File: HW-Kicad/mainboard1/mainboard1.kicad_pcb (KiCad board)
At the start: 2 copper layers, 101 x 101 mm, 17 parts, among them J1 Conn_01x03_Male, J2 Conn_01x02_Male, J3 Conn_01x07_Male, J4 Conn_01x04_Male, J5 Conn_01x04_Male, J8 Conn_02x10_Odd_Even, U1 MCP1700-2802E_TO92, U2 ESP32-WROOM-E, U3 Mini360, U4 YAAJ_DCDC_StepDown_LM2596

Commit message: agregue texto para foto
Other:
- board text added: "10v Rx Tx GND"
- board text added: "GND TX RX 10V"
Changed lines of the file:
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@@
   (gr_line (start 214.24 140.7) (end 119.24 140.7) (layer "Edge.Cuts") (width 0.2))
   (gr_circle (center 207.365 43.825) (end 208.865 43.825) (layer "Edge.Cuts") (width 0.2) (fill none))
+  (gr_text "10v\nRx\nTx\nGND" (at 192.7 47.2) (layer "B.SilkS")
+    (effects (font (size 2 2) (thickness 0.15)) (justify mirror))
+  )
+  (gr_text "GND\nTX\nRX\n10V" (at 142.4 47.6) (layer "B.SilkS")
+    (effects (font (size 2 2) (thickness 0.15)) (justify mirror))
+  )
   (segment (start 170.7 65.1) (end 165.874 60.274) (width 0.8) (layer "F.Cu") (net 1))
   (segment (start 191.1 65.1) (end 170.7 65.1) (width 0.8) (layer "F.Cu") (net 1))

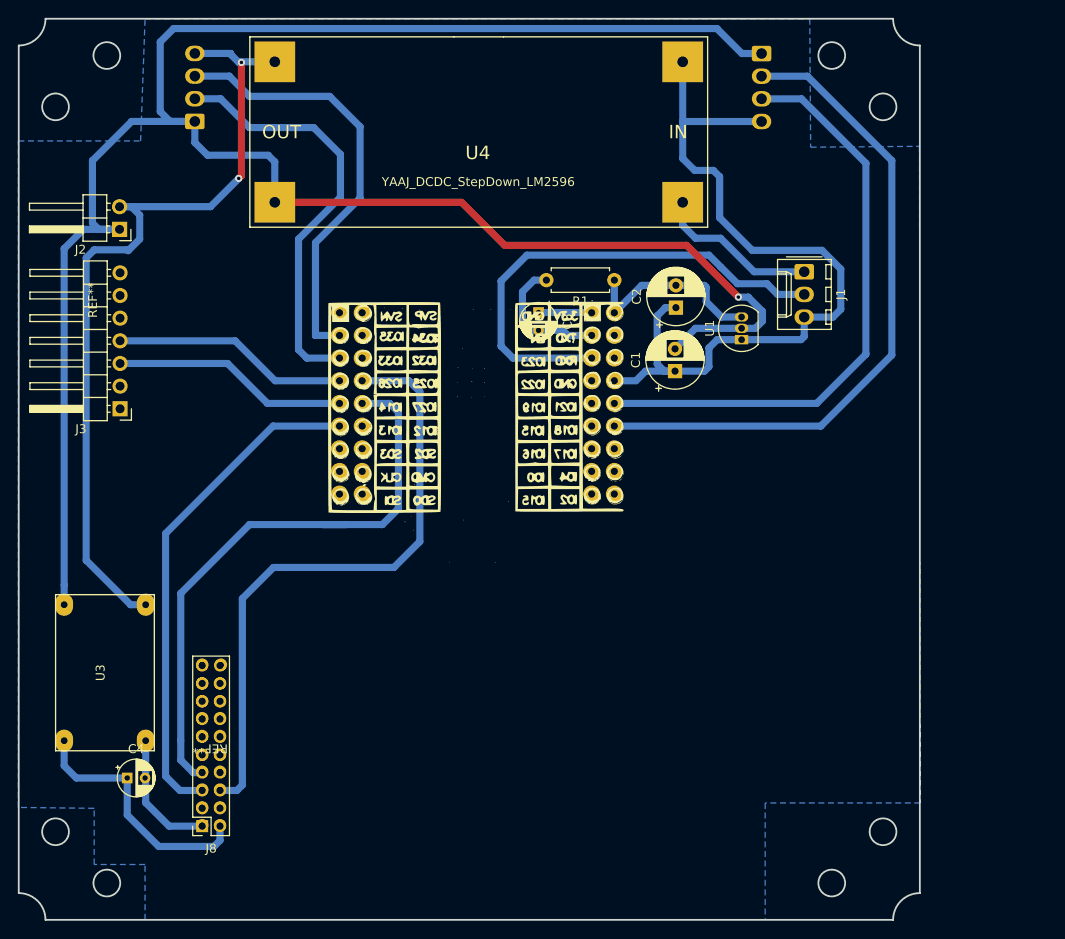
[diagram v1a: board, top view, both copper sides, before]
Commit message: actualicé pines del esp32
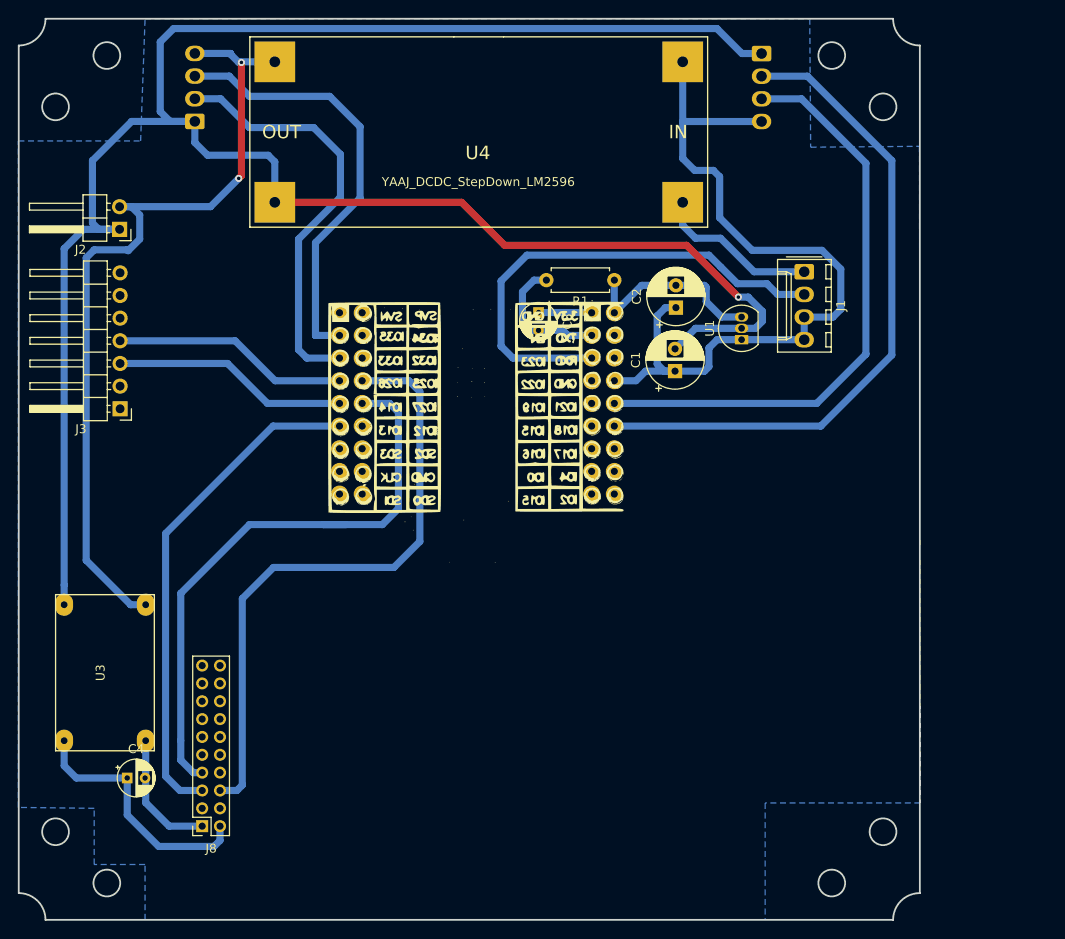
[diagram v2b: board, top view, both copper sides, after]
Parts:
- removed REF**: 9xtend, 9xtend:9xtend
- removed REF**: LightAPRS, LightAPRS:LightAPRS
- J1: value Conn_01x03_Male -> Conn_01x04_Male; footprint Connector_Molex:Molex_KK-254_AE-6410-03A_1x03_P2.54mm_Vertical -> Connector_Molex:Molex_KK-254_AE-6410-04A_1x04_P2.54mm_Vertical
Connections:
- J1 pad 3: GND -> paracaidas
- U2 pad 10: xtendTX -> unconnected-(U2-Pad10)
- U2 pad 16: xtendRX -> unconnected-(U2-Pad16)
- U2 pad 34: unconnected-(U2-Pad34) -> xtendTX
- U2 pad 35: unconnected-(U2-Pad35) -> xtendRX
- U2 pad 36: unconnected-(U2-Pad36) -> paracaidas
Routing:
- net xtendTX: track 70.0 -> 0.00 mm
- net unconnected-(U2-Pad10): track 0.00 -> 70.0 mm
- net xtendRX: track 56.4 -> 0.00 mm
- net unconnected-(U2-Pad16): track 0.00 -> 56.4 mm

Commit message: importe nueva version de leo
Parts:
- removed U3: Mini360, mini360:Mini360_step-down
- added C10: 100n, Capacitor_THT:C_Disc_D3.4mm_W2.1mm_P2.50mm, F.Cu at (206.8, 93.5)
- added C5: 100n, Capacitor_THT:C_Disc_D3.4mm_W2.1mm_P2.50mm, F.Cu at (208.3, 90.2)
- added C6: 100n, Capacitor_THT:C_Disc_D3.4mm_W2.1mm_P2.50mm, F.Cu at (146.8, 50.8)
- added C7: 100n, Capacitor_THT:C_Disc_D3.4mm_W2.1mm_P2.50mm, F.Cu at (186.2, 50.8)
- added C8: 100u, Capacitor_THT:CP_Radial_D6.3mm_P2.50mm, F.Cu at (142.2, 76.2)
- added C9: 100n, Capacitor_THT:C_Disc_D3.4mm_W2.1mm_P2.50mm, F.Cu at (196.1, 93.5)
- added D1: 1N4148, Diode_THT:D_DO-35_SOD27_P7.62mm_Horizontal, F.Cu at (193.3, 95.8)
- added D2: 1N4148, Diode_THT:D_DO-35_SOD27_P7.62mm_Horizontal, F.Cu at (193.8, 87.9)
- added F1: Polyfuse, Resistor_THT:R_Axial_DIN0207_L6.3mm_D2.5mm_P5.08mm_Vertical, F.Cu at (137.4, 71.9)
- added F2: Polyfuse, Resistor_THT:R_Axial_DIN0207_L6.3mm_D2.5mm_P5.08mm_Vertical, F.Cu at (197.1, 63.0)
- added HS1: Heatsink, Library:9xtend, F.Cu at (137.8, 121.2)
- added Q1: BC337, Package_TO_SOT_THT:TO-92_Inline_Wide, F.Cu at (159.5, 100.3)
- added Q2: IRF9540N, Package_TO_SOT_THT:TO-220-3_Vertical, F.Cu at (137.3, 62.2)
- added Q3: BC337, Package_TO_SOT_THT:TO-92_Inline_Wide, F.Cu at (169.3, 95.2)
- added Q4: BC337, Package_TO_SOT_THT:TO-92_Inline_Wide, F.Cu at (164.7, 100.3)
- added Q5: IRF9540N, Package_TO_SOT_THT:TO-220-3_Vertical, F.Cu at (205.2, 62.5)
- added Q6: BC337, Package_TO_SOT_THT:TO-92_Inline_Wide, F.Cu at (174.5, 95.2)
- added R10: 4.7k, Resistor_THT:R_Axial_DIN0207_L6.3mm_D2.5mm_P7.62mm_Horizontal, F.Cu at (157.0, 61.0)
- added R11: 4.7k, Resistor_THT:R_Axial_DIN0207_L6.3mm_D2.5mm_P7.62mm_Horizontal, F.Cu at (177.3, 61.0)
- added R12: 10k, Resistor_THT:R_Axial_DIN0207_L6.3mm_D2.5mm_P7.62mm_Horizontal, F.Cu at (163.6, 84.1)
- added R13: 10k, Resistor_THT:R_Axial_DIN0207_L6.3mm_D2.5mm_P7.62mm_Horizontal, F.Cu at (140.5, 63.5)
- added R14: 100k, Resistor_THT:R_Axial_DIN0207_L6.3mm_D2.5mm_P7.62mm_Horizontal, F.Cu at (199.4, 88.4)
- added R15: 1, Resistor_THT:R_Axial_DIN0207_L6.3mm_D2.5mm_P7.62mm_Horizontal, F.Cu at (156.5, 43.4)
- added R16: 10k, Resistor_THT:R_Axial_DIN0207_L6.3mm_D2.5mm_P7.62mm_Horizontal, F.Cu at (199.4, 106.7)
- added R17: 1, Resistor_THT:R_Axial_DIN0207_L6.3mm_D2.5mm_P7.62mm_Horizontal, F.Cu at (153.2, 51.1)
- added R18: 10k, Resistor_THT:R_Axial_DIN0207_L6.3mm_D2.5mm_P7.62mm_Horizontal, F.Cu at (160.3, 84.1)
- added R19: 10k, Resistor_THT:R_Axial_DIN0207_L6.3mm_D2.5mm_P7.62mm_Horizontal, F.Cu at (167.0, 84.1)
- added R2: 100k, Resistor_THT:R_Axial_DIN0207_L6.3mm_D2.5mm_P7.62mm_Horizontal, F.Cu at (149.9, 51.1)
- added R20: 10k, Resistor_THT:R_Axial_DIN0207_L6.3mm_D2.5mm_P7.62mm_Horizontal, F.Cu at (209.3, 64.5)
- added R21: 100k, Resistor_THT:R_Axial_DIN0207_L6.3mm_D2.5mm_P7.62mm_Horizontal, F.Cu at (203.2, 88.4)
- added R22: 10k, Resistor_THT:R_Axial_DIN0207_L6.3mm_D2.5mm_P7.62mm_Horizontal, F.Cu at (203.2, 106.7)
- added R23: 1, Resistor_THT:R_Axial_DIN0207_L6.3mm_D2.5mm_P7.62mm_Horizontal, F.Cu at (176.8, 43.4)
- added R24: 10k, Resistor_THT:R_Axial_DIN0207_L6.3mm_D2.5mm_P7.62mm_Horizontal, F.Cu at (170.4, 84.1)
- added R25: 1, Resistor_THT:R_Axial_DIN0207_L6.3mm_D2.5mm_P7.62mm_Horizontal, F.Cu at (180.1, 51.1)
- added R3: 100k, Resistor_THT:R_Axial_DIN0207_L6.3mm_D2.5mm_P7.62mm_Horizontal, F.Cu at (183.1, 51.1)
- added R4: 100k, Resistor_THT:R_Axial_DIN0207_L6.3mm_D2.5mm_P7.62mm_Horizontal, F.Cu at (159.8, 43.4)
- added R5: 100k, Resistor_THT:R_Axial_DIN0207_L6.3mm_D2.5mm_P7.62mm_Horizontal, F.Cu at (173.2, 43.4)
- added R6: 3.3k, Resistor_THT:R_Axial_DIN0207_L6.3mm_D2.5mm_P7.62mm_Horizontal, F.Cu at (149.4, 57.7)
- added R7: 3.3k, Resistor_THT:R_Axial_DIN0207_L6.3mm_D2.5mm_P7.62mm_Horizontal, F.Cu at (184.9, 57.7)
- added R8: 10k, Resistor_THT:R_Axial_DIN0207_L6.3mm_D2.5mm_P7.62mm_Horizontal, F.Cu at (149.4, 54.4)
- added R9: 10k, Resistor_THT:R_Axial_DIN0207_L6.3mm_D2.5mm_P7.62mm_Horizontal, F.Cu at (184.9, 54.1)
- added U5: LM7805_TO220, Package_TO_SOT_THT:TO-220-3_Vertical, F.Cu at (206.8, 80.5)
- added U6: LM324, Package_DIP:DIP-14_W7.62mm, F.Cu at (162.6, 44.4)
- added U7: HEF4093B, Package_DIP:DIP-14_W7.62mm, F.Cu at (175.5, 73.2)
- C1, C2: value 100u -> 100n; footprint Capacitor_THT:CP_Radial_D6.3mm_P2.50mm -> Capacitor_THT:C_Disc_D3.4mm_W2.1mm_P2.50mm
- C4: value 100uF -> 470uF; footprint Capacitor_THT:CP_Radial_D4.0mm_P2.00mm -> Capacitor_THT:CP_Radial_D8.0mm_P3.80mm
- U1: footprint Package_TO_SOT_THT:TO-92_Inline -> Package_TO_SOT_THT:TO-92_Inline_Wide
- moved C1 13.4 mm to (197.6, 68.3)
- moved C3 12.6 mm to (186.7, 69.6), turned to 90 degrees
- moved C2 7.03 mm to (194.8, 67.1), turned to -90 degrees
- moved U1 4.42 mm to (196.4, 80.0)
- moved C4 4.12 mm to (125.5, 121.9)
- moved R1 1.69 mm to (183.0, 67.3)
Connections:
- C4 pad 1: Net-(C4-Pad1) -> VBAT
- C4 pad 2: Net-(C4-Pad2) -> GND
- J4 pad 1: VBAT -> VCC_protect_1
- J4 pad 4: GND -> GND_protect_1
- J5 pad 1: VBAT -> VCC_protect_2
- J5 pad 4: GND -> GND_protect_2
- J8 pad 1: Net-(C4-Pad2) -> GND
- J8 pad 2: Net-(C4-Pad1) -> VBAT
- U2 pad 27: unconnected-(U2-Pad27) -> uC_activation_FF1
- U2 pad 28: unconnected-(U2-Pad28) -> uC_activation_FF2
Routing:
- net +5V: track 0.00 -> 188.3 mm, vias 0 -> 10
- net xtendRX: track 0.00 -> 131.6 mm, vias 0 -> 12
- net xtendTX: track 0.00 -> 106.4 mm, vias 0 -> 4
- net Net-(Q4-Pad1): track 0.00 -> 102.3 mm, vias 0 -> 4
- net paracaidas: track 0.00 -> 80.5 mm, vias 0 -> 4
- net unconnected-(U2-Pad10): track 70.0 -> 0.00 mm
- net Net-(U7-Pad13): track 0.00 -> 61.1 mm, vias 0 -> 4
- net GND: track 189.4 -> 248.8 mm, vias 2 -> 25
- net Net-(Q1-Pad1): track 0.00 -> 59.4 mm, vias 0 -> 6
- net unconnected-(U2-Pad16): track 56.4 -> 0.00 mm
- net Net-(C10-Pad2): track 0.00 -> 43.1 mm, vias 0 -> 2
- net Net-(C9-Pad2): track 0.00 -> 42.8 mm
- net abortSig: track 55.0 -> 91.0 mm, vias 0 -> 6
- net FF_R2: track 0.00 -> 30.7 mm, vias 0 -> 2
- net GND_protect_1: track 0.00 -> 30.2 mm
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
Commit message: agegue el conector de energía separado para el aprs
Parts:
- added J6: Conn_01x02_Male, Connector_PinHeader_2.54mm:PinHeader_1x02_P2.54mm_Vertical, F.Cu at (121.5, 63.3)
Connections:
- J2 pad 1: VBAT -> APRSBATT
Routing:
- net VBAT: track 211.9 -> 172.1 mm
- net APRSBATT: track 0.00 -> 6.06 mm
- net GND: track 248.8 -> 254.9 mm
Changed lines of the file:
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@@
   (net 86 "uC_activation_FF1")
   (net 87 "uC_activation_FF2")
+  (net 88 "APRSBATT")
   (footprint "Package_TO_SOT_THT:TO-92_Inline_Wide" (layer "F.Cu")
     (at 196.448 80.01 90)
@@
     (fp_line (start -0.32 0.32) (end 1.5 0.32) (layer "F.Fab") (width 0.1))
     (pad "1" thru_hole rect (at 0 0 180) (size 1.7 1.7) (drill 1) (layers *.Cu *.Mask)
-      (net 1 "VBAT") (pinfunction "Pin_1") (pintype "passive"))
+      (net 88 "APRSBATT") (pinfunction "Pin_1") (pintype "passive"))
     (pad "2" thru_hole oval (at 0 2.54 180) (size 1.7 1.7) (drill 1) (layers *.Cu *.Mask)
       (net 2 "GND") (pinfunction "Pin_2") (pintype "passive"))
@@
     )
   )
+  (footprint "Connector_PinHeader_2.54mm:PinHeader_1x02_P2.54mm_Vertical" (layer "F.Cu")
+    (at 121.5 63.275 180)
+    (descr "Through hole straight pin header, 1x02, 2.54mm pitch, single row")
+    (tags "Through hole pin header THT 1x02 2.54mm single row")
+    (property "Sheetfile" "mainboard1.kicad_sch")
+    (property "Sheetname" "")
+    (attr through_hole)
+    (fp_text reference "J6" (at 0 -2.33) (layer "F.SilkS")
+      (effects (font (size 1 1) (thickness 0.15)))
+    )
+    (fp_text value "Conn_01x02_Male" (at 0 4.87) (layer "F.Fab")
+      (effects (font (size 1 1) (thickness 0.15)))
+    )
+    (fp_text user "${REFERENCE}" (at 0 1.27 90) (layer "F.Fab")
+      (effects (font (size 1 1) (thickness 0.15)))
+    )
+    (fp_line (start 1.33 1.27) (end 1.33 3.87) (layer "F.SilkS") (width 0.12))
+    (fp_line (start -1.33 1.27) (end 1.33 1.27) (layer "F.SilkS") (width 0.12))
+    (fp_line (start -1.33 1.27) (end -1.33 3.87) (layer "F.SilkS") (width 0.12))
+    (fp_line (start -1.33 -1.33) (end 0 -1.33) (layer "F.SilkS") (width 0.12))
+    (fp_line (start -1.33 3.87) (end 1.33 3.87) (layer "F.SilkS") (width 0.12))
+    (fp_line (start -1.33 0) (end -1.33 -1.33) (layer "F.SilkS") (width 0.12))
+    (fp_line (start -1.8 -1.8) (end -1.8 4.35) (layer "F.CrtYd") (width 0.05))
+    (fp_line (start -1.8 4.35) (end 1.8 4.35) (layer "F.CrtYd") (width 0.05))
+    (fp_line (start 1.8 -1.8) (end -1.8 -1.8) (layer "F.CrtYd") (width 0.05))
+    (fp_line (start 1.8 4.35) (end 1.8 -1.8) (layer "F.CrtYd") (width 0.05))
+    (fp_line (start 1.27 -1.27) (end 1.27 3.81) (layer "F.Fab") (width 0.1))
+    (fp_line (start -0.635 -1.27) (end 1.27 -1.27) (layer "F.Fab") (width 0.1))
+    (fp_line (start -1.27 3.81) (end -1.27 -0.635) (layer "F.Fab") (width 0.1))
+    (fp_line (start -1.27 -0.635) (end -0.635 -1.27) (layer "F.Fab") (width 0.1))
+    (fp_line (start 1.27 3.81) (end -1.27 3.81) (layer "F.Fab") (width 0.1))
+    (pad "1" thru_hole rect (at 0 0 180) (size 1.7 1.7) (drill 1) (layers *.Cu *.Mask)
+      (net 88 "APRSBATT") (pinfunction "Pin_1") (pintype "passive"))
+    (pad "2" thru_hole oval (at 0 2.54 180) (size 1.7 1.7) (drill 1) (layers *.Cu *.Mask)
+      (net 2 "GND") (pinfunction "Pin_2") (pintype "passive"))
+    (model "${KICAD6_3DMODEL_DIR}/Connector_PinHeader_2.54mm.3dshapes/PinHeader_1x02_P2.54mm_Vertical.wrl"
+      (offset (xyz 0 0 0))
+      (scale (xyz 1 1 1))
+      (rotate (xyz 0 0 0))
+    )
+  )
   (footprint "Capacitor_THT:CP_Radial_D4.0mm_P2.00mm" (layer "F.Cu")
     (at 186.69 69.564 90)
@@
   (segment (start 139.192 92.456) (end 139.192 87.376) (width 0.8) (layer "B.Cu") (net 1))
   (segment (start 125.451349 106.196651) (end 139.192 92.456) (width 0.8) (layer "B.Cu") (net 1))
-  (segment (start 137.668 86.106) (end 136.906 86.106) (width 0.8) (layer "B.Cu") (net 1))
   (segment (start 125.451349 121.92) (end 125.451349 125.996549) (width 0.8) (layer "B.Cu") (net 1))
   (segment (start 137.922 86.106) (end 137.668 86.106) (width 0.8) (layer "B.Cu") (net 1))
   (segment (start 138.1274 132.4726) (end 138.8 131.8) (width 0.8) (layer "B.Cu") (net 1))
-  (segment (start 124.46 64.516) (end 125.671 63.305) (width 0.8) (layer "B.Cu") (net 1))
   (segment (start 125.451349 125.996549) (end 131.9274 132.4726) (width 0.8) (layer "B.Cu") (net 1))
   (segment (start 137.414 71.911) (end 142.973 71.911) (width 0.8) (layer "B.Cu") (net 1))
@@
   (segment (start 197.612 63.5) (end 197.104 62.992) (width 0.8) (layer "B.Cu") (net 1))
   (segment (start 200.152 64.77) (end 200.152 68.58) (width 0.8) (layer "B.Cu") (net 1))
-  (segment (start 124.46 86.36) (end 124.46 64.516) (width 0.8) (layer "B.Cu") (net 1))
   (segment (start 148.082 66.802) (end 148.082 66.04) (width 0.8) (layer "B.Cu") (net 1))
   (segment (start 146.558 65.532) (end 147.574 65.532) (width 1.2) (layer "B.Cu") (net 1))
@@
   (segment (start 198.374 62.992) (end 200.152 64.77) (width 0.8) (layer "B.Cu") (net 1))
   (segment (start 142.973 71.911) (end 148.082 66.802) (width 0.8) (layer "B.Cu") (net 1))
-  (segment (start 136.906 86.106) (end 135.382 87.63) (width 0.8) (layer "B.Cu") (net 1))
-  (segment (start 125.671 63.305) (end 127.545 63.305) (width 0.8) (layer "B.Cu") (net 1))
   (segment (start 131.9274 132.4726) (end 138.1274 132.4726) (width 0.8) (layer "B.Cu") (net 1))
-  (segment (start 135.382 87.63) (end 125.73 87.63) (width 0.8) (layer "B.Cu") (net 1))
   (segment (start 137.414 73.914) (end 137.414 75.692) (width 0.8) (layer "B.Cu") (net 1))
   (segment (start 137.414 71.911) (end 137.414 73.914) (width 0.8) (layer "B.Cu") (net 1))
-  (segment (start 125.73 87.63) (end 124.46 86.36) (width 0.8) (layer "B.Cu") (net 1))
   (segment (start 144.94 63.914) (end 146.558 65.532) (width 1.2) (layer "B.Cu") (net 1))
   (segment (start 182.995 80.275) (end 182.637 80.275) (width 0.2) (layer "F.Cu") (net 2))
@@
   (via (at 180.848 99.822) (size 1) (drill 0.7) (layers "F.Cu" "B.Cu") (net 2))
   (via (at 204.724 82.296) (size 1) (drill 0.7) (layers "F.Cu" "B.Cu") (net 2))
+  (segment (start 121.5 60.735) (end 127.515 60.735) (width 0.8) (layer "B.Cu") (net 2))
   (segment (start 188.722 52.578) (end 188.722 50.8) (width 0.8) (layer "B.Cu") (net 2))
   (segment (start 205.76 90.19) (end 209.042 93.472) (width 0.8) (layer "B.Cu") (net 2))
@@
   (segment (start 177.038 99.822) (end 176.53 100.33) (width 0.8) (layer "B.Cu") (net 2))
   (segment (start 189.23 67.056) (end 186.722 69.564) (width 0.8) (layer "B.Cu") (net 2))
+  (segment (start 127.515 60.735) (end 127.545 60.765) (width 0.8) (layer "B.Cu") (net 2))
   (segment (start 161.29 71.628) (end 161.29 68.072) (width 0.8) (layer "B.Cu") (net 2))
   (segment (start 158.496 66.802) (end 156.21 69.088) (width 0.8) (layer "B.Cu") (net 2))
@@
   (segment (start 183.006 87.884) (end 182.995 87.895) (width 0.8) (layer "B.Cu") (net 87))
   (segment (start 186.182 87.884) (end 183.006 87.884) (width 0.8) (layer "B.Cu") (net 87))
+  (segment (start 127.515 63.275) (end 127.545 63.305) (width 0.8) (layer "B.Cu") (net 88))
+  (segment (start 121.5 63.275) (end 127.515 63.275) (width 0.8) (layer "B.Cu") (net 88))
   (zone (net 2) (net_name "GND") (layer "B.Cu") (hatch edge 0.508)
     (connect_pads yes (clearance 0.508))

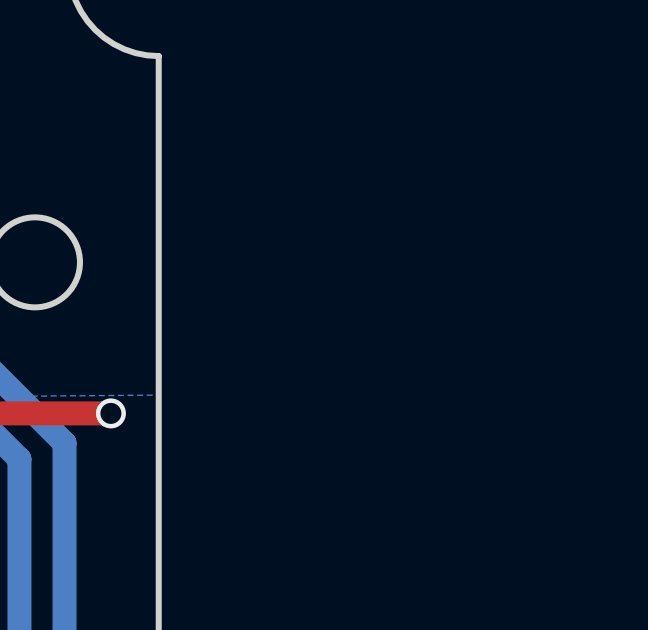
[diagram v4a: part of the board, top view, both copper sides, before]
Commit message: correcciones
resistencias en operacionales no inversores de medición de corriente y MOSFET invertidos
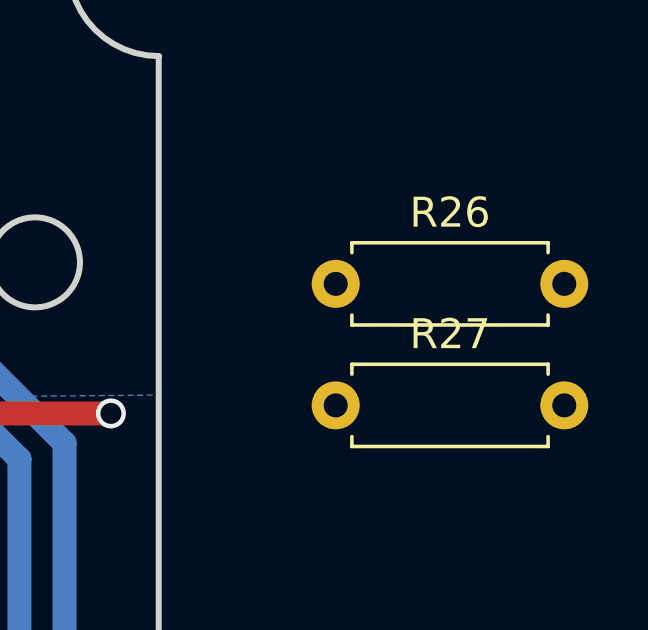
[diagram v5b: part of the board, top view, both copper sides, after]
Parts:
- added R26: 10k, Resistor_THT:R_Axial_DIN0207_L6.3mm_D2.5mm_P7.62mm_Horizontal, F.Cu at (223.1, 50.3)
- added R27: 10k, Resistor_THT:R_Axial_DIN0207_L6.3mm_D2.5mm_P7.62mm_Horizontal, F.Cu at (223.1, 54.3)
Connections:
- Q2 pad 2: Net-(F1-Pad2) -> VCC_protect_1
- Q2 pad 3: VCC_protect_1 -> Net-(F1-Pad2)
- Q5 pad 2: Net-(F2-Pad2) -> VCC_protect_2
- Q5 pad 3: VCC_protect_2 -> Net-(F2-Pad2)
- U2 pad 16: unconnected-(U2-Pad16) -> Q1
- U2 pad 6: unconnected-(U2-Pad6) -> Q2
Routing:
- net Net-(F1-Pad2): track 17.3 -> 23.8 mm
- net VCC_protect_1: track 6.50 -> 0.00 mm
